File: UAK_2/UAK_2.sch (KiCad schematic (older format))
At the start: 56 parts, among them K1 Кнопка_FSMSM, K2 Кнопка_FSMSM, X1 Крепежное_отверстие_М3, X2 Крепежное_отверстие_М3, X3 Крепежное_отверстие_М3, X4 Крепежное_отверстие_М3

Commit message: добавлена методика программирования, на схему вынесен новый дисплей
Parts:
- added HL?: TFT-дисплей_ST7735_ILI9341, symbol elements_2020:TFT-дисплей_ST7735_ILI9341
- C2: symbol UAK_1-rescue:Конденсатор_К53-56А-32В-22_мкФ+-10проц.-MOTOR_2020_components-UAK_0-rescue -> UAK_2-rescue:Конденсатор_К53-56А-32В-22_мкФ+-10проц.-MOTOR_2020_components-UAK_0-rescue-UAK_1-rescue
- DA1: symbol UAK_1-rescue:МОП-реле_КР293КП1Б-elements_2020-UAK_0-rescue -> UAK_2-rescue:МОП-реле_КР293КП1Б-elements_2020-UAK_0-rescue-UAK_1-rescue
- DD1: symbol UAK_1-rescue:Повторитель_M74VHC1GT125-elements_2020-UAK_0-rescue -> UAK_2-rescue:Повторитель_M74VHC1GT125-elements_2020-UAK_0-rescue-UAK_1-rescue
- HA1: symbol UAK_1-rescue:Излучатель_HPA17F-elements_2020-UAK_0-rescue -> UAK_2-rescue:Излучатель_HPA17F-elements_2020-UAK_0-rescue-UAK_1-rescue
- HL1: symbol UAK_1-rescue:Жидкокристалический_индикатор_MT-16S2H-2KLW-elements_2020-UAK_0-rescue -> UAK_2-rescue:Жидкокристалический_индикатор_MT-16S2H-2KLW-elements_2020-UAK_0-rescue-UAK_1-rescue
- RP1: symbol UAK_1-rescue:Резистор_подстроечный_PVA3A103-elements_2020-UAK_0-rescue -> UAK_2-rescue:Резистор_подстроечный_PVA3A103-elements_2020-UAK_0-rescue-UAK_1-rescue
- VD1: symbol UAK_1-rescue:Диод_шоттки_SK16-elements_2020-UAK_0-rescue -> UAK_2-rescue:Диод_шоттки_SK16-elements_2020-UAK_0-rescue-UAK_1-rescue
- VD3: symbol UAK_1-rescue:Набор_диодов_2Д803АС9-MOTOR_2020_components-UAK_0-rescue -> UAK_2-rescue:Набор_диодов_2Д803АС9-MOTOR_2020_components-UAK_0-rescue-UAK_1-rescue
- VT1, VT2, VT3, VT4: symbol UAK_1-rescue:Транзистор_полевой_N-канальный_IRLML6344TR-elements_2020-UAK_0-rescue -> UAK_2-rescue:Транзистор_полевой_N-канальный_IRLML6344TR-elements_2020-UAK_0-rescue-UAK_1-rescue
- X1, X2, X3, X4: symbol UAK_1-rescue:Крепежное_отверстие_М3-MOTOR_2020_components-UAK_0-rescue -> UAK_2-rescue:Крепежное_отверстие_М3-MOTOR_2020_components-UAK_0-rescue-UAK_1-rescue
- XFU1, XFU2: symbol UAK_1-rescue:Держатель_предохранителя_KLS5-266-elements_2020 -> UAK_2-rescue:Держатель_предохранителя_KLS5-266-elements_2020-UAK_1-rescue
- XP1: symbol UAK_1-rescue:Вилка_СНП389-4ВП32-1-1-MOTOR_2020_components-UAK_0-rescue -> UAK_2-rescue:Вилка_СНП389-4ВП32-1-1-MOTOR_2020_components-UAK_0-rescue-UAK_1-rescue
- XT1, XT2, XT3, XT4, XT6, XT7, XT8: symbol UAK_1-rescue:Клеммник_х2_KLS2-300-5.00-02P-2S-elements_2020-UAK_0-rescue -> UAK_2-rescue:Клеммник_х2_KLS2-300-5.00-02P-2S-elements_2020-UAK_0-rescue-UAK_1-rescue
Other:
- note added: "заменить на SOT-23"
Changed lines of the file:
@@
 EESchema Schematic File Version 4
-LIBS:UAK_1-cache
+LIBS:UAK_2-cache
 EELAYER 29 0
 EELAYER END
@@
 $EndComp
 $Comp
-L UAK_1-rescue:Клеммник_х2_KLS2-300-5.00-02P-2S-elements_2020-UAK_0-rescue XT4
+L UAK_2-rescue:Клеммник_х2_KLS2-300-5.00-02P-2S-elements_2020-UAK_0-rescue-UAK_1-rescue XT4
 U 1 1 5F53E542
 P 14750 1500
@@
 	14500 4750 14100 4750
 $Comp
-L UAK_1-rescue:Набор_диодов_2Д803АС9-MOTOR_2020_components-UAK_0-rescue VD3
+L UAK_2-rescue:Набор_диодов_2Д803АС9-MOTOR_2020_components-UAK_0-rescue-UAK_1-rescue VD3
 U 1 1 5F55ECC5
 P 13500 5800
@@
 BOOT_UART_RX
 $Comp
-L UAK_1-rescue:Вилка_СНП389-4ВП32-1-1-MOTOR_2020_components-UAK_0-rescue XP1
+L UAK_2-rescue:Вилка_СНП389-4ВП32-1-1-MOTOR_2020_components-UAK_0-rescue-UAK_1-rescue XP1
 U 1 1 5F5606D4
 P 15000 5900
@@
 	13000 8000 13000 7500
 $Comp
-L UAK_1-rescue:Клеммник_х2_KLS2-300-5.00-02P-2S-elements_2020-UAK_0-rescue XT6
+L UAK_2-rescue:Клеммник_х2_KLS2-300-5.00-02P-2S-elements_2020-UAK_0-rescue-UAK_1-rescue XT6
 U 1 1 5F598429
 P 14500 7500
@@
 КОНЦЕВИК ДВЕРИ
 $Comp
-L UAK_1-rescue:Транзистор_полевой_N-канальный_IRLML6344TR-elements_2020-UAK_0-rescue VT2
+L UAK_2-rescue:Транзистор_полевой_N-канальный_IRLML6344TR-elements_2020-UAK_0-rescue-UAK_1-rescue VT2
 U 1 1 5F5AB6F0
 P 9000 2000
@@
 GND
 $Comp
-L UAK_1-rescue:Клеммник_х2_KLS2-300-5.00-02P-2S-elements_2020-UAK_0-rescue XT1
+L UAK_2-rescue:Клеммник_х2_KLS2-300-5.00-02P-2S-elements_2020-UAK_0-rescue-UAK_1-rescue XT1
 U 1 1 5F5B9CF4
 P 10750 1550
@@
 12V
 $Comp
-L UAK_1-rescue:Диод_шоттки_SK16-elements_2020-UAK_0-rescue VD1
+L UAK_2-rescue:Диод_шоттки_SK16-elements_2020-UAK_0-rescue-UAK_1-rescue VD1
 U 1 1 5F5C4406
 P 9750 1500
@@
 	4950 2450 5500 2450
 $Comp
-L UAK_1-rescue:Крепежное_отверстие_М3-MOTOR_2020_components-UAK_0-rescue X4
+L UAK_2-rescue:Крепежное_отверстие_М3-MOTOR_2020_components-UAK_0-rescue-UAK_1-rescue X4
 U 1 1 5F5D023C
 P 11000 10500
@@
 $EndComp
 $Comp
-L UAK_1-rescue:Крепежное_отверстие_М3-MOTOR_2020_components-UAK_0-rescue X3
+L UAK_2-rescue:Крепежное_отверстие_М3-MOTOR_2020_components-UAK_0-rescue-UAK_1-rescue X3
 U 1 1 5F5D0231
 P 10500 10500
@@
 $EndComp
 $Comp
-L UAK_1-rescue:Крепежное_отверстие_М3-MOTOR_2020_components-UAK_0-rescue X2
+L UAK_2-rescue:Крепежное_отверстие_М3-MOTOR_2020_components-UAK_0-rescue-UAK_1-rescue X2
 U 1 1 5F5CFEAE
 P 10000 10500
@@
 $EndComp
 $Comp
-L UAK_1-rescue:Крепежное_отверстие_М3-MOTOR_2020_components-UAK_0-rescue X1
+L UAK_2-rescue:Крепежное_отверстие_М3-MOTOR_2020_components-UAK_0-rescue-UAK_1-rescue X1
 U 1 1 5F5CFB44
 P 9500 10500
@@
 	10000 5700 9250 5700
 $Comp
-L UAK_1-rescue:Резистор_подстроечный_PVA3A103-elements_2020-UAK_0-rescue RP1
+L UAK_2-rescue:Резистор_подстроечный_PVA3A103-elements_2020-UAK_0-rescue-UAK_1-rescue RP1
 U 1 1 5F651E48
 P 9300 5100
@@
 $EndComp
 $Comp
-L UAK_1-rescue:Транзистор_полевой_N-канальный_IRLML6344TR-elements_2020-UAK_0-rescue VT1
+L UAK_2-rescue:Транзистор_полевой_N-канальный_IRLML6344TR-elements_2020-UAK_0-rescue-UAK_1-rescue VT1
 U 1 1 5F61B72E
 P 8950 7300
@@
 	9750 3950 11000 3950
 $Comp
-L UAK_1-rescue:Излучатель_HPA17F-elements_2020-UAK_0-rescue HA1
+L UAK_2-rescue:Излучатель_HPA17F-elements_2020-UAK_0-rescue-UAK_1-rescue HA1
 U 1 1 5F5EFC61
 P 11100 3850
@@
 $EndComp
 $Comp
-L UAK_1-rescue:Транзистор_полевой_N-канальный_IRLML6344TR-elements_2020-UAK_0-rescue VT3
+L UAK_2-rescue:Транзистор_полевой_N-канальный_IRLML6344TR-elements_2020-UAK_0-rescue-UAK_1-rescue VT3
 U 1 1 5F5E6E4B
 P 9000 4250
@@
 $EndComp
 $Comp
-L UAK_1-rescue:Жидкокристалический_индикатор_MT-16S2H-2KLW-elements_2020-UAK_0-rescue HL1
+L UAK_2-rescue:Жидкокристалический_индикатор_MT-16S2H-2KLW-elements_2020-UAK_0-rescue-UAK_1-rescue HL1
 U 1 1 5F5D943F
 P 10000 5500
@@
 	13000 9500 13000 9000
 $Comp
-L UAK_1-rescue:Клеммник_х2_KLS2-300-5.00-02P-2S-elements_2020-UAK_0-rescue XT7
+L UAK_2-rescue:Клеммник_х2_KLS2-300-5.00-02P-2S-elements_2020-UAK_0-rescue-UAK_1-rescue XT7
 U 1 1 5F5BFDD6
 P 10750 2250
@@
 NoConn ~ 1500 3400
 $Comp
-L UAK_1-rescue:Повторитель_M74VHC1GT125-elements_2020-UAK_0-rescue DD1
+L UAK_2-rescue:Повторитель_M74VHC1GT125-elements_2020-UAK_0-rescue-UAK_1-rescue DD1
 U 1 1 5F73F35E
 P 9100 9500
@@
 5V
 $Comp
-L UAK_1-rescue:Конденсатор_К53-56А-32В-22_мкФ+-10проц.-MOTOR_2020_components-UAK_0-rescue C2
+L UAK_2-rescue:Конденсатор_К53-56А-32В-22_мкФ+-10проц.-MOTOR_2020_components-UAK_0-rescue-UAK_1-rescue C2
 U 1 1 5F75AF76
 P 10000 8650
@@
 	4950 1400 5500 1400
 $Comp
-L UAK_1-rescue:Клеммник_х2_KLS2-300-5.00-02P-2S-elements_2020-UAK_0-rescue XT2
+L UAK_2-rescue:Клеммник_х2_KLS2-300-5.00-02P-2S-elements_2020-UAK_0-rescue-UAK_1-rescue XT2
 U 1 1 5F79F40F
 P 10750 8750
@@
 $EndComp
 $Comp
-L UAK_1-rescue:Клеммник_х2_KLS2-300-5.00-02P-2S-elements_2020-UAK_0-rescue XT3
+L UAK_2-rescue:Клеммник_х2_KLS2-300-5.00-02P-2S-elements_2020-UAK_0-rescue-UAK_1-rescue XT3
 U 1 1 5F7A0B62
 P 14500 9000
@@
 НА СВЕТОДИОДНУЮ ЛЕНТУ WS2812
 $Comp
-L UAK_1-rescue:Клеммник_х2_KLS2-300-5.00-02P-2S-elements_2020-UAK_0-rescue XT8
+L UAK_2-rescue:Клеммник_х2_KLS2-300-5.00-02P-2S-elements_2020-UAK_0-rescue-UAK_1-rescue XT8
 U 1 1 5F5696D9
 P 5750 7000
@@
 $EndComp
 $Comp
-L UAK_1-rescue:МОП-реле_КР293КП1Б-elements_2020-UAK_0-rescue DA1
+L UAK_2-rescue:МОП-реле_КР293КП1Б-elements_2020-UAK_0-rescue-UAK_1-rescue DA1
 U 1 1 5F56E7B1
 P 4100 5900
@@
 $EndComp
 $Comp
-L UAK_1-rescue:Транзистор_полевой_N-канальный_IRLML6344TR-elements_2020-UAK_0-rescue VT4
+L UAK_2-rescue:Транзистор_полевой_N-канальный_IRLML6344TR-elements_2020-UAK_0-rescue-UAK_1-rescue VT4
 U 1 1 5F5D0EF1
 P 3000 6650
@@
 5V
 $Comp
-L UAK_1-rescue:Держатель_предохранителя_KLS5-266-elements_2020 XFU1
+L UAK_2-rescue:Держатель_предохранителя_KLS5-266-elements_2020-UAK_1-rescue XFU1
 U 1 1 5F802810
 P 13750 1500
@@
 $EndComp
 $Comp
-L UAK_1-rescue:Держатель_предохранителя_KLS5-266-elements_2020 XFU2
+L UAK_2-rescue:Держатель_предохранителя_KLS5-266-elements_2020-UAK_1-rescue XFU2
 U 1 1 5F8032F7
 P 14500 1500
@@
 Text Label 6000 1250 2    50   ~ 0
 MOSI
+$Comp
+L elements_2020:TFT-дисплей_ST7735_ILI9341 HL?
+U 1 1 5F9F74B5
+P 2500 8500
+F 0 "HL?" H 3050 8650 50  0000 L CNN
+F 1 "TFT-дисплей_ST7735_ILI9341" H 2700 6400 50  0000 L CNN
+F 2 "" H 2500 8500 50  0001 C CNN
+F 3 "" H 2500 8500 50  0001 C CNN
+	1    2500 8500
+	1    0    0    -1
+$EndComp
+Text Notes 9000 9250 0    50   ~ 0
+заменить на SOT-23
 $EndSCHEMATC

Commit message: UAK.2A.MN + PDF +STEP
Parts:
- HL1: footprint N_VD_HL:ЖК_MT-16S2H -> N_VD_HL:ЖК_MT-16S2H_2DRL
- HL2: renamed from HL?; footprint (none) -> N_VD_HL:TFT_2.8_INCH
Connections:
- net 5V: now also HL2.1 (VCC)
- net GND: now also HL2.2 (GND)
- net LCD_A0: now also HL2.14 (TOUCH_IRQ)
- net LCD_DATA_4: now also HL2.5 (TFT_DC)
- net LCD_DATA_5: now also HL2.3 (TFT_CD)
- net LCD_DATA_6: now also HL2.10 (TOUCH_CLK), HL2.7 (TFT_SCLK)
- net LCD_DATA_7: now also HL2.13 (TOUCH_MISO), HL2.9 (TFT_MISO)
- net LCD_E: now also HL2.11 (TOUCH_CS)
- net LCD_LED: now also HL2.8 (TFT_LED)
- net MOSI: now also HL2.12 (TOUCH_MOSI), HL2.6 (TFT_MOSI)
- net TFT_RES: now reaches A1.14 (IO12)
- net TFT_RES: now also HL2.4 (TFT_RES)
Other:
- note removed: "заменить на SOT-23"
- moved on the sheet: A1
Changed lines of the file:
@@
 EESchema Schematic File Version 4
 LIBS:UAK_2-cache
-EELAYER 29 0
+EELAYER 30 0
 EELAYER END
 $Descr A3 16535 11693
@@
 L modules:модуль_esp32_wrover_OR_wroom32_SMD A1
 U 1 1 5F5375C0
-P 1700 1000
-F 0 "A1" H 3250 1200 50  0000 C CNN
-F 1 "модуль_esp32_wrover_OR_wroom32_SMD" H 3350 -2000 50  0000 C CNN
-F 2 "N_A:ESP32_WROVER_or_WROOM32" H 1700 1000 50  0001 C CNN
-F 3 "" H 1700 1000 50  0001 C CNN
-F 4 "https://www.terraelectronica.ru/product/2292549" H 1700 1000 50  0001 C CNN "LINK"
-F 5 "ESP32-WROOM-32 [4MB]" H 1700 1000 50  0001 C CNN "Для заказа"
-	1    1700 1000
+P 1950 1000
+F 0 "A1" H 3500 1200 50  0000 C CNN
+F 1 "модуль_esp32_wrover_OR_wroom32_SMD" H 3600 -2000 50  0000 C CNN
+F 2 "N_A:ESP32_WROVER_or_WROOM32" H 1950 1000 50  0001 C CNN
+F 3 "" H 1950 1000 50  0001 C CNN
+F 4 "https://www.terraelectronica.ru/product/2292549" H 1950 1000 50  0001 C CNN "LINK"
+F 5 "ESP32-WROOM-32 [4MB]" H 1950 1000 50  0001 C CNN "Для заказа"
+	1    1950 1000
 	1    0    0    -1
 $EndComp
@@
 F7 "12V" I L 12250 1500 50
 $EndSheet
-Text Label 1000 1300 0    50   ~ 0
+Text Label 1250 1300 0    50   ~ 0
 EN_RESET
 Wire Wire Line
-	1500 1300 1000 1300
+	1750 1300 1250 1300
 Wire Wire Line
 	12250 2000 12000 2000
@@
 Text Label 12000 2000 0    50   ~ 0
 3V3
-Text Label 1000 1000 0    50   ~ 0
-GND
-Text Label 1000 1150 0    50   ~ 0
+Text Label 1250 1000 0    50   ~ 0
+GND
+Text Label 1250 1150 0    50   ~ 0
 3V3
 Wire Wire Line
-	1500 1150 1000 1150
-Wire Wire Line
-	1500 1000 1000 1000
-Text Label 5500 3050 2    50   ~ 0
+	1750 1150 1250 1150
+Wire Wire Line
+	1750 1000 1250 1000
+Text Label 5750 3050 2    50   ~ 0
 BOOT_SEL
 Wire Wire Line
-	5500 3050 4950 3050
+	5750 3050 5200 3050
 $Comp
 L elements:кнопка K1
@@
 Text Label 12000 4250 0    50   ~ 0
 EN_RESET
-Text Label 5500 1550 2    50   ~ 0
+Text Label 5750 1550 2    50   ~ 0
 BOOT_UART_TX
 Wire Wire Line
-	5500 1550 4950 1550
-Text Label 5500 1700 2    50   ~ 0
+	5750 1550 5200 1550
+Text Label 5750 1700 2    50   ~ 0
 BOOT_UART_RX
 Wire Wire Line
-	5500 1700 4950 1700
+	5750 1700 5200 1700
 Text Label 12000 4750 0    50   ~ 0
 BOOT_SEL
@@
 Text Label 12000 1750 0    50   ~ 0
 5V
-Text Label 5500 1850 2    50   ~ 0
+Text Label 5750 1850 2    50   ~ 0
 BUZZER
-Text Label 1000 2500 0    50   ~ 0
+Text Label 1250 2500 0    50   ~ 0
 MC_OUT_1
 Wire Wire Line
-	1000 2500 1500 2500
-Text Label 1000 3100 0    50   ~ 0
-GND
-Wire Wire Line
-	1500 3100 1000 3100
-Text Label 5500 950  2    50   ~ 0
-GND
-Wire Wire Line
-	4950 950  5500 950
-Text Label 5500 1100 2    50   ~ 0
-GND
-Wire Wire Line
-	4950 1100 5500 1100
-Text Label 5500 2600 2    50   ~ 0
+	1250 2500 1750 2500
+Text Label 1250 3100 0    50   ~ 0
+GND
+Wire Wire Line
+	1750 3100 1250 3100
+Text Label 5750 950  2    50   ~ 0
+GND
+Wire Wire Line
+	5200 950  5750 950
+Text Label 5750 1100 2    50   ~ 0
+GND
+Wire Wire Line
+	5200 1100 5750 1100
+Text Label 5750 2600 2    50   ~ 0
 DOOR_SENSOR
-Text Label 1000 3250 0    50   ~ 0
+Text Label 1250 3250 0    50   ~ 0
 LCD_LED
-Text Label 5500 3350 2    50   ~ 0
+Text Label 5750 3350 2    50   ~ 0
 LCD_A0
-Text Label 5500 3200 2    50   ~ 0
+Text Label 5750 3200 2    50   ~ 0
 LCD_E
-Wire Wire Line
-	4950 3350 5500 3350
-Wire Wire Line
-	4950 3200 5500 3200
-Text Label 5500 2900 2    50   ~ 0
+Text Label 5750 2900 2    50   ~ 0
 LCD_DATA_4
-Text Label 5500 2450 2    50   ~ 0
+Text Label 5750 2450 2    50   ~ 0
 LCD_DATA_5
-Text Label 5500 2300 2    50   ~ 0
+Text Label 5750 2300 2    50   ~ 0
 LCD_DATA_6
-Text Label 5500 2150 2    50   ~ 0
+Text Label 5750 2150 2    50   ~ 0
 LCD_DATA_7
-Wire Wire Line
-	4950 2900 5500 2900
-Wire Wire Line
-	4950 2450 5500 2450
 $Comp
 L UAK_2-rescue:Крепежное_отверстие_М3-MOTOR_2020_components-UAK_0-rescue-UAK_1-rescue X4
@@
 F 0 "HL1" H 11000 5650 50  0000 L CNN
 F 1 "Жидкокристалический_индикатор_MT-16S2H-2KLW" H 10625 3425 50  0001 C CNN
-F 2 "N_VD_HL:ЖК_MT-16S2H" H 10000 5725 50  0001 C CNN
+F 2 "N_VD_HL:ЖК_MT-16S2H_2DRL" H 10000 5725 50  0001 C CNN
 F 3 "http://www.melt.com.ru/docs/MT-16S2H.pdf" H 10000 5500 50  0001 C CNN
 F 4 "-" H 10000 5500 50  0001 C CNN "Для заказа"
@@
 Text Notes 11900 8750 0    50   ~ 0
 ВНЕШНЯЯ КНОПКА
-Text Label 1000 2650 0    50   ~ 0
+Text Label 1250 2650 0    50   ~ 0
 EXT_BUTTON
 Wire Notes Line
@@
 	11750 7000 11750 8250
 Wire Wire Line
-	4950 1850 5500 1850
-Wire Wire Line
-	1000 2650 1500 2650
-Wire Wire Line
-	1500 3250 1000 3250
-NoConn ~ 4950 2750
-NoConn ~ 1500 3550
-NoConn ~ 1500 3400
+	5200 1850 5750 1850
+Wire Wire Line
+	1250 2650 1750 2650
+NoConn ~ 5200 2750
+NoConn ~ 1750 3550
+NoConn ~ 1750 3400
 $Comp
 L UAK_2-rescue:Повторитель_M74VHC1GT125-elements_2020-UAK_0-rescue-UAK_1-rescue DD1
@@
 Wire Wire Line
 	8500 9600 9000 9600
-Text Label 5500 1400 2    50   ~ 0
+Text Label 5750 1400 2    50   ~ 0
 LED_WS2812
 Wire Wire Line
-	4950 1400 5500 1400
+	5200 1400 5750 1400
 $Comp
 L UAK_2-rescue:Клеммник_х2_KLS2-300-5.00-02P-2S-elements_2020-UAK_0-rescue-UAK_1-rescue XT2
@@
 Wire Wire Line
 	3750 5900 3750 6350
-Text Label 1000 2350 0    50   ~ 0
+Text Label 1250 2350 0    50   ~ 0
 MC_220_OUT
 Wire Wire Line
-	1000 2350 1500 2350
+	1250 2350 1750 2350
 $Comp
 L elements:Резистор_0,25Вт R22
@@
 	1    0    0    -1
 $EndComp
-Text Label 6000 2150 2    50   ~ 0
+Text Label 6250 2150 2    50   ~ 0
 MISO
-Text Label 6000 2300 2    50   ~ 0
+Text Label 6250 2300 2    50   ~ 0
 SCK
 Wire Wire Line
-	4950 2150 6000 2150
-Wire Wire Line
-	4950 2300 6000 2300
-Wire Wire Line
-	4950 2600 5500 2600
-Wire Wire Line
-	4950 1250 6000 1250
-Text Label 6000 1250 2    50   ~ 0
+	5200 2150 6250 2150
+Wire Wire Line
+	5200 2300 6250 2300
+Wire Wire Line
+	5200 2600 5750 2600
+Wire Wire Line
+	5200 1250 6250 1250
+Text Label 6250 1250 2    50   ~ 0
 MOSI
 $Comp
-L elements_2020:TFT-дисплей_ST7735_ILI9341 HL?
+L elements_2020:TFT-дисплей_ST7735_ILI9341 HL2
 U 1 1 5F9F74B5
 P 2500 8500
-F 0 "HL?" H 3050 8650 50  0000 L CNN
-F 1 "TFT-дисплей_ST7735_ILI9341" H 2700 6400 50  0000 L CNN
-F 2 "" H 2500 8500 50  0001 C CNN
+F 0 "HL2" H 3050 8650 50  0000 L CNN
+F 1 "TFT-дисплей_ST7735_ILI9341" H 2400 6400 50  0000 L CNN
+F 2 "N_VD_HL:TFT_2.8_INCH" H 2500 8500 50  0001 C CNN
 F 3 "" H 2500 8500 50  0001 C CNN
 	1    2500 8500
 	1    0    0    -1
 $EndComp
-Text Notes 9000 9250 0    50   ~ 0
-заменить на SOT-23
+Text Label 2000 8800 0    50   ~ 0
+TFT_CS
+Text Label 2000 9100 0    50   ~ 0
+TFT_DC
+Text Label 2000 8950 0    50   ~ 0
+TFT_RES
+Text Label 2000 9550 0    50   ~ 0
+TFT_LED
+Text Label 2000 9250 0    50   ~ 0
+MOSI
+Text Label 2000 9700 0    50   ~ 0
+MISO
+Text Label 2000 9400 0    50   ~ 0
+SCK
+Wire Wire Line
+	2500 8800 2000 8800
+Wire Wire Line
+	2500 8950 2000 8950
+Wire Wire Line
+	2500 9100 2000 9100
+Wire Wire Line
+	2500 9250 2000 9250
+Wire Wire Line
+	2500 9400 2000 9400
+Wire Wire Line
+	2500 9550 2000 9550
+Wire Wire Line
+	2500 9700 2000 9700
+Text Label 2000 8650 0    50   ~ 0
+GND
+Wire Wire Line
+	2500 8650 2000 8650
+Text Label 2000 8500 0    50   ~ 0
+5V
+Wire Wire Line
+	2000 8500 2500 8500
+Text Label 6250 2450 2    50   ~ 0
+TFT_CS
+Text Label 6250 2900 2    50   ~ 0
+TFT_DC
+Text Label 1250 2950 0    50   ~ 0
+TFT_RES
+Wire Wire Line
+	5200 2450 6250 2450
+Wire Wire Line
+	1250 2950 1750 2950
+Wire Wire Line
+	750  3250 1750 3250
+Text Label 750  3250 0    50   ~ 0
+TFT_LED
+Wire Wire Line
+	5200 2900 6250 2900
+Text Label 2000 10300 0    50   ~ 0
+MISO
+Wire Wire Line
+	2500 10300 2000 10300
+Text Label 2000 10150 0    50   ~ 0
+MOSI
+Wire Wire Line
+	2500 10150 2000 10150
+Text Label 2000 9850 0    50   ~ 0
+SCK
+Wire Wire Line
+	2500 9850 2000 9850
+Text Label 2000 10000 0    50   ~ 0
+TOUCH_CS
+Wire Wire Line
+	2500 10000 2000 10000
+Text Label 6250 3200 2    50   ~ 0
+TOUCH_CS
+Wire Wire Line
+	5200 3200 6250 3200
+Text Label 2000 10450 0    50   ~ 0
+TOUCH_IRQ
+Wire Wire Line
+	2500 10450 2000 10450
+Text Label 6250 3350 2    50   ~ 0
+TOUCH_IRQ
+Wire Wire Line
+	5200 3350 6250 3350
 $EndSCHEMATC

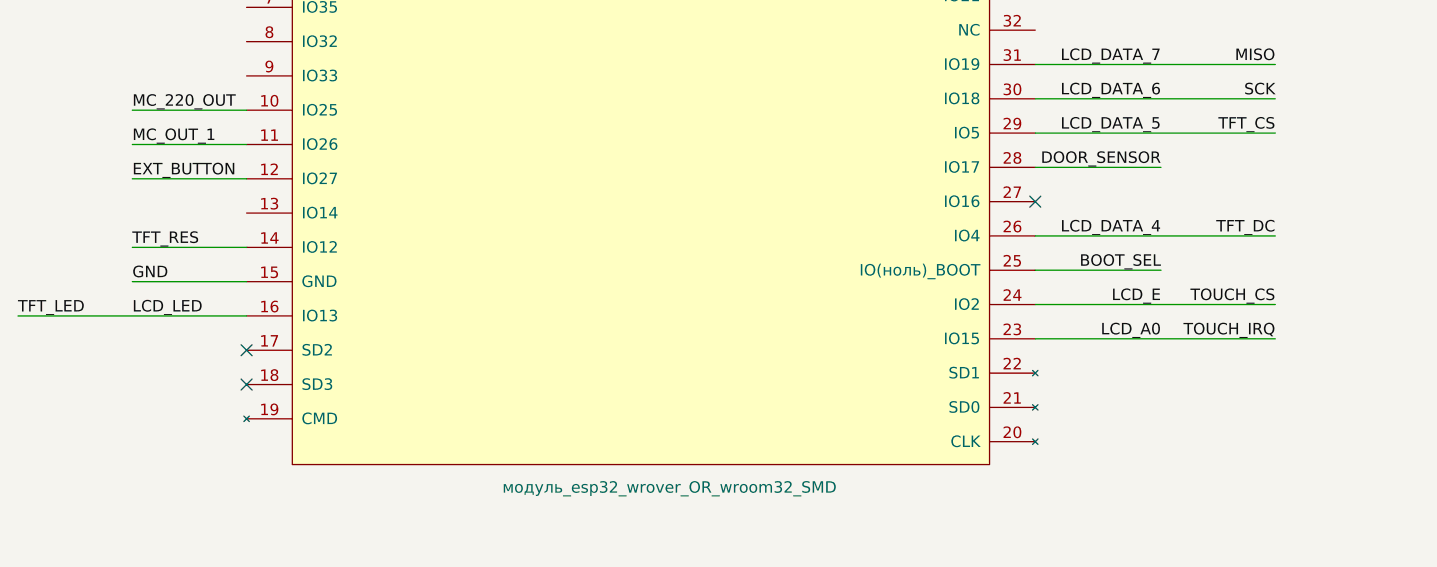
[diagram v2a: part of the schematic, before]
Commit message: заменен буфер, перекинуты ножки контроллера,, обновлены PCB +STEP +PDF
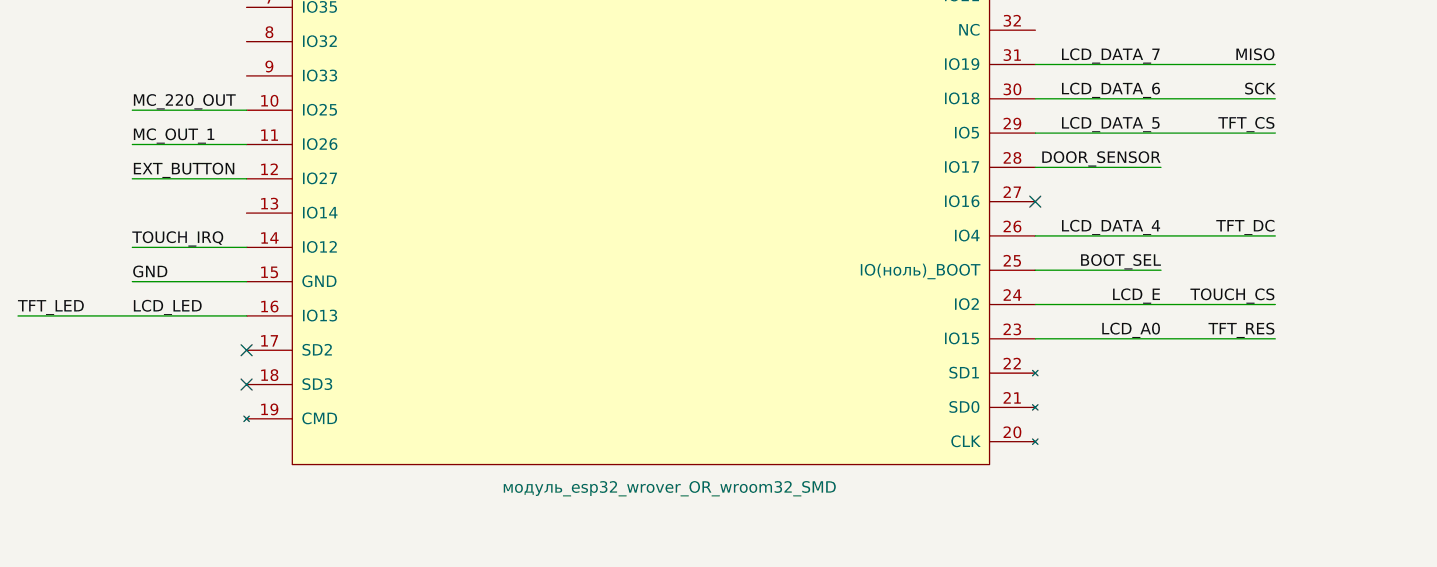
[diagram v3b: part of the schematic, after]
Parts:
- DD1: footprint N_DD:SC-70-5 -> N_G:Преобразователь_LM2703_SOT-23-5; LINK https://www.terraelectronica.ru/product/274803 -> https://www.terraelectronica.ru/product/287011; Для заказа Повторитель M74VHC1GT125DF2G -> Повторитель M74VHC1GT125DT1G
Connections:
- net LCD_A0: now also HL2.4 (TFT_RES); no longer HL2.14 (TOUCH_IRQ)
- net TFT_RES renamed TOUCH_IRQ
- net TOUCH_IRQ: now also HL2.14 (TOUCH_IRQ); no longer HL2.4 (TFT_RES)
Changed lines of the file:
@@
 encoding utf-8
 Sheet 1 2
-Title "UAK.1C.M9"
+Title "UAK.2B.MN"
 Date ""
 Rev ""
@@
 F 0 "DD1" H 9450 9650 50  0000 C CNN
 F 1 "Повторитель_M74VHC1GT125" H 9350 9150 50  0000 C CNN
-F 2 "N_DD:SC-70-5" H 9125 8950 50  0001 C CNN
+F 2 "N_G:Преобразователь_LM2703_SOT-23-5" H 9125 8950 50  0001 C CNN
 F 3 "https://static.chipdip.ru/lib/225/DOC000225700.pdf" H 9100 9500 50  0001 C CNN
-F 4 "https://www.terraelectronica.ru/product/274803" H 9125 9050 50  0001 C CNN "LINK"
-F 5 "Повторитель M74VHC1GT125DF2G" H 9100 9500 50  0001 C CNN "Для заказа"
+F 4 "https://www.terraelectronica.ru/product/287011" H 9125 9050 50  0001 C CNN "LINK"
+F 5 "Повторитель M74VHC1GT125DT1G" H 9100 9500 50  0001 C CNN "Для заказа"
 	1    9100 9500
 	1    0    0    -1
@@
 Text Label 6250 2900 2    50   ~ 0
 TFT_DC
-Text Label 1250 2950 0    50   ~ 0
+Text Label 6250 3350 2    50   ~ 0
 TFT_RES
 Wire Wire Line
@@
 Wire Wire Line
 	2500 10450 2000 10450
-Text Label 6250 3350 2    50   ~ 0
+Text Label 1250 2950 0    50   ~ 0
 TOUCH_IRQ
 Wire Wire Line
